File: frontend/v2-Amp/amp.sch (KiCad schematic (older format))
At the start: 69 parts, among them K1 HK4100, P1 Antenna, P2 CONN_02X06, P4 TX-IN, P5 RX IN, P6 12-13.8v, Q1 2N3688A, Q2 RD16HHF1, T1 OUT_TRANSF, T2 OUT_TRANSF, U1 LP2951-50D

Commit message: Completion of Norton addition
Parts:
- removed Q1: 2N3688A, HERMESLITE:TO39EBC, symbol NPN
- removed R13: 51, Resistors_SMD:R_0805_HandSoldering, symbol R
- removed T2: OUT_TRANSF, Pin_Headers:Pin_Header_Straight_2x02, symbol OUT_TRANSF
- added Q1: PZT2222A, TO_SOT_Packages_SMD:SOT-223, symbol PZT2222A-T
- added T2: BN-43-2402, HERMESLITE:TRANSF, symbol TRANSFO2
- R11: value 470 -> 1k
- R18: value 4.7 -> 47
- R9: value 2k -> 1k
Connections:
- wire segments 110 -> 112
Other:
- note added: "1T #30\n"
- note added: "3T #30\n"
- note added: "5T #30\n"
- note added: "Atten R8/12 R10\n dB Ohms Ohms\n 1 910 5.6\n 2 430 12\n 3 270 18\n 4 220 24\n 5 180 30"
- note added: "Attenuator (3db example) needed \nto ensure that input impedance\nof Norton amplifier is 50 ohms."
- note removed: "Attenuator\n(3db example)"
- note removed: "FT37-43\n2x10T #30"
- moved on the sheet: C12, P4, R11, R18, R9
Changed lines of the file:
@@
 	1    0    0    -1
 $EndComp
-Text Notes 4000 3600 0    50   ~ 0
-  Attenuator\n(3db example)
+Text Notes 3450 4650 0    50   ~ 0
+Attenuator (3db example) needed \nto ensure that input impedance\nof Norton amplifier is 50 ohms.
 $Comp
 L INDUCTOR L1
@@
 L CONN_01X02 P4
 U 1 1 55CE52FF
-P 1750 4050
-F 0 "P4" H 1750 4200 50  0000 C CNN
-F 1 "TX-IN" H 1750 3850 50  0000 C CNN
-F 2 "Pin_Headers:Pin_Header_Straight_1x02" H 1750 4050 60  0001 C CNN
-F 3 "" H 1750 4050 60  0000 C CNN
-	1    1750 4050
+P 1250 3950
+F 0 "P4" H 1250 4100 50  0000 C CNN
+F 1 "TX-IN" H 1250 3750 50  0000 C CNN
+F 2 "Pin_Headers:Pin_Header_Straight_1x02" H 1250 3950 60  0001 C CNN
+F 3 "" H 1250 3950 60  0000 C CNN
+	1    1250 3950
 	-1   0    0    1
 $EndComp
@@
 $EndComp
 Wire Wire Line
-	1950 4100 2000 4100
-Wire Wire Line
-	2000 4100 2000 4200
+	1450 4000 1500 4000
+Wire Wire Line
+	1500 4000 1500 4100
 $Comp
 L GND #PWR017
 U 1 1 55D1DC89
-P 2000 4200
-F 0 "#PWR017" H 2000 4200 30  0001 C CNN
-F 1 "GND" H 2000 4130 30  0001 C CNN
-F 2 "" H 2000 4200 60  0000 C CNN
-F 3 "" H 2000 4200 60  0000 C CNN
-	1    2000 4200
+P 1500 4100
+F 0 "#PWR017" H 1500 4100 30  0001 C CNN
+F 1 "GND" H 1500 4030 30  0001 C CNN
+F 2 "" H 1500 4100 60  0000 C CNN
+F 3 "" H 1500 4100 60  0000 C CNN
+	1    1500 4100
 	1    0    0    -1
 $EndComp
@@
 	2150 1250 8800 1250
 $Comp
-L NPN Q1
-U 1 1 55E46016
-P 2550 4000
-F 0 "Q1" H 2550 3850 50  0000 R CNN
-F 1 "2N3688A" H 3050 3850 50  0000 R CNN
-F 2 "HERMESLITE:TO39EBC" H 2550 4000 60  0001 C CNN
-F 3 "" H 2550 4000 60  0000 C CNN
-	1    2550 4000
-	1    0    0    -1
-$EndComp
-$Comp
 L R R9
 U 1 1 55E46597
-P 2350 3750
-F 0 "R9" V 2430 3750 40  0000 C CNN
-F 1 "2k" V 2357 3751 40  0000 C CNN
-F 2 "Resistors_SMD:R_0805_HandSoldering" V 2280 3750 30  0001 C CNN
-F 3 "" H 2350 3750 30  0000 C CNN
-	1    2350 3750
+P 2250 4300
+F 0 "R9" V 2330 4300 40  0000 C CNN
+F 1 "1k" V 2257 4301 40  0000 C CNN
+F 2 "Resistors_SMD:R_0805_HandSoldering" V 2180 4300 30  0001 C CNN
+F 3 "" H 2250 4300 30  0000 C CNN
+	1    2250 4300
 	-1   0    0    1
 $EndComp
@@
 L R R11
 U 1 1 55E46614
-P 2350 4250
-F 0 "R11" V 2430 4250 40  0000 C CNN
-F 1 "470" V 2357 4251 40  0000 C CNN
-F 2 "Resistors_SMD:R_0805_HandSoldering" V 2280 4250 30  0001 C CNN
-F 3 "" H 2350 4250 30  0000 C CNN
-	1    2350 4250
+P 2250 4800
+F 0 "R11" V 2150 4800 40  0000 C CNN
+F 1 "1k" V 2257 4801 40  0000 C CNN
+F 2 "Resistors_SMD:R_0805_HandSoldering" V 2180 4800 30  0001 C CNN
+F 3 "" H 2250 4800 30  0000 C CNN
+	1    2250 4800
 	-1   0    0    1
 $EndComp
@@
 L C C12
 U 1 1 55E46682
-P 2150 4000
-F 0 "C12" V 2200 4050 40  0000 L CNN
-F 1 "0.1uF" H 2150 3900 40  0000 L CNN
-F 2 "HERMESLITE:C_0805" H 2188 3850 30  0001 C CNN
-F 3 "" H 2150 4000 60  0000 C CNN
-	1    2150 4000
+P 1650 3900
+F 0 "C12" V 1700 3950 40  0000 L CNN
+F 1 "0.1uF" V 1750 3650 40  0000 L CNN
+F 2 "HERMESLITE:C_0805" H 1688 3750 30  0001 C CNN
+F 3 "" H 1650 3900 60  0000 C CNN
+	1    1650 3900
 	0    -1   -1   0
 $EndComp
 Connection ~ 3650 1250
-$Comp
-L OUT_TRANSF T2
-U 1 1 55E46E76
-P 3150 3500
-F 0 "T2" H 3150 3750 70  0000 C CNN
-F 1 "OUT_TRANSF" H 3150 3200 70  0000 C CNN
-F 2 "Pin_Headers:Pin_Header_Straight_2x02" H 3150 3500 60  0001 C CNN
-F 3 "" H 3150 3500 60  0000 C CNN
-	1    3150 3500
-	1    0    0    -1
-$EndComp
-Wire Wire Line
-	2650 3500 2650 3800
-Wire Wire Line
-	2650 3700 2750 3700
-Wire Wire Line
-	2650 3500 2350 3500
-Connection ~ 2650 3700
 $Comp
 L C C86
@@
 P 3750 3700
 F 0 "C86" V 3800 3750 40  0000 L CNN
-F 1 "0.1uF" H 3750 3600 40  0000 L CNN
+F 1 "0.1uF" V 3850 3450 40  0000 L CNN
 F 2 "HERMESLITE:C_0805" H 3788 3550 30  0001 C CNN
 F 3 "" H 3750 3700 60  0000 C CNN
@@
 	3800 3300 3550 3300
 Connection ~ 3800 1600
-Wire Wire Line
-	3550 3700 3550 3500
-Wire Wire Line
-	3550 3500 3600 3500
-Wire Wire Line
-	3600 3500 3600 3100
-Wire Wire Line
-	3600 3100 2750 3100
-Wire Wire Line
-	2750 3100 2750 3300
 $Comp
 L C C87
@@
 $EndComp
 Wire Wire Line
-	2650 4200 2650 4250
-Wire Wire Line
-	2550 4250 2750 4250
-Wire Wire Line
-	2550 4250 2550 4350
-Wire Wire Line
-	2750 4250 2750 4350
-Connection ~ 2650 4250
-$Comp
-L R R13
-U 1 1 55E4824A
-P 2550 4600
-F 0 "R13" V 2630 4600 40  0000 C CNN
-F 1 "51" V 2557 4601 40  0000 C CNN
-F 2 "Resistors_SMD:R_0805_HandSoldering" V 2480 4600 30  0001 C CNN
-F 3 "" H 2550 4600 30  0000 C CNN
-	1    2550 4600
-	-1   0    0    1
-$EndComp
+	2550 4750 2550 4800
 $Comp
 L R R18
 U 1 1 55E483BD
-P 2750 4600
-F 0 "R18" V 2830 4600 40  0000 C CNN
-F 1 "4.7" V 2757 4601 40  0000 C CNN
-F 2 "Resistors_SMD:R_0805_HandSoldering" V 2680 4600 30  0001 C CNN
-F 3 "" H 2750 4600 30  0000 C CNN
-	1    2750 4600
-	-1   0    0    1
-$EndComp
-$Comp
-L C C85
-U 1 1 55E484B3
-P 2750 5050
-F 0 "C85" V 2800 5100 40  0000 L CNN
-F 1 "0.1uF" H 2750 4950 40  0000 L CNN
-F 2 "HERMESLITE:C_0805" H 2788 4900 30  0001 C CNN
-F 3 "" H 2750 5050 60  0000 C CNN
-	1    2750 5050
+P 2550 5050
+F 0 "R18" V 2630 5050 40  0000 C CNN
+F 1 "47" V 2557 5051 40  0000 C CNN
+F 2 "Resistors_SMD:R_0805_HandSoldering" V 2480 5050 30  0001 C CNN
+F 3 "" H 2550 5050 30  0000 C CNN
+	1    2550 5050
 	-1   0    0    1
 $EndComp
@@
 L GND #PWR029
 U 1 1 55E488C1
-P 2350 4500
-F 0 "#PWR029" H 2350 4500 30  0001 C CNN
-F 1 "GND" H 2350 4430 30  0001 C CNN
-F 2 "" H 2350 4500 60  0000 C CNN
-F 3 "" H 2350 4500 60  0000 C CNN
-	1    2350 4500
+P 2250 5050
+F 0 "#PWR029" H 2250 5050 30  0001 C CNN
+F 1 "GND" H 2250 4980 30  0001 C CNN
+F 2 "" H 2250 5050 60  0000 C CNN
+F 3 "" H 2250 5050 60  0000 C CNN
+	1    2250 5050
 	1    0    0    -1
 $EndComp
@@
 L GND #PWR030
 U 1 1 55E48911
-P 2750 5250
-F 0 "#PWR030" H 2750 5250 30  0001 C CNN
-F 1 "GND" H 2750 5180 30  0001 C CNN
-F 2 "" H 2750 5250 60  0000 C CNN
-F 3 "" H 2750 5250 60  0000 C CNN
-	1    2750 5250
-	1    0    0    -1
-$EndComp
-$Comp
-L GND #PWR031
-U 1 1 55E48961
-P 2550 4850
-F 0 "#PWR031" H 2550 4850 30  0001 C CNN
-F 1 "GND" H 2550 4780 30  0001 C CNN
-F 2 "" H 2550 4850 60  0000 C CNN
-F 3 "" H 2550 4850 60  0000 C CNN
-	1    2550 4850
-	1    0    0    -1
-$EndComp
-Text Notes 3100 4050 0    50   ~ 0
-FT37-43\n2x10T #30
+P 2550 5300
+F 0 "#PWR030" H 2550 5300 30  0001 C CNN
+F 1 "GND" H 2550 5230 30  0001 C CNN
+F 2 "" H 2550 5300 60  0000 C CNN
+F 3 "" H 2550 5300 60  0000 C CNN
+	1    2550 5300
+	1    0    0    -1
+$EndComp
 Wire Wire Line
 	2400 2500 3250 2500
@@
 Wire Wire Line
 	1700 2000 1900 2000
+$Comp
+L PZT2222A-T Q1
+U 1 1 55E99EC8
+P 2450 4550
+F 0 "Q1" H 2450 4402 40  0000 R CNN
+F 1 "PZT2222A" H 2700 4800 40  0000 R CNN
+F 2 "TO_SOT_Packages_SMD:SOT-223" H 3000 4250 29  0001 C CNN
+F 3 "" H 2450 4550 60  0000 C CNN
+	1    2450 4550
+	1    0    0    -1
+$EndComp
+Wire Wire Line
+	2550 4350 3650 4350
+$Comp
+L C C85
+U 1 1 55EA0F85
+P 2050 4750
+F 0 "C85" V 2100 4800 40  0000 L CNN
+F 1 "0.1uF" H 1850 4650 40  0000 L CNN
+F 2 "HERMESLITE:C_0805" H 2088 4600 30  0001 C CNN
+F 3 "" H 2050 4750 60  0000 C CNN
+	1    2050 4750
+	1    0    0    -1
+$EndComp
+$Comp
+L GND #PWR031
+U 1 1 55EA100D
+P 2050 4950
+F 0 "#PWR031" H 2050 4950 30  0001 C CNN
+F 1 "GND" H 2050 4880 30  0001 C CNN
+F 2 "" H 2050 4950 60  0000 C CNN
+F 3 "" H 2050 4950 60  0000 C CNN
+	1    2050 4950
+	1    0    0    -1
+$EndComp
+Wire Wire Line
+	2050 4550 2250 4550
+$Comp
+L TRANSFO2 T2
+U 1 1 55EA135A
+P 3150 3700
+F 0 "T2" H 3150 4200 70  0000 C CNN
+F 1 "BN-43-2402" H 3200 3150 70  0000 C CNN
+F 2 "HERMESLITE:TRANSF" H 3150 3700 60  0001 C CNN
+F 3 "" H 3150 3700 60  0000 C CNN
+	1    3150 3700
+	1    0    0    -1
+$EndComp
+Wire Wire Line
+	3550 3600 3550 3800
+Connection ~ 3550 3700
+Wire Wire Line
+	3650 4350 3650 4100
+Wire Wire Line
+	3650 4100 3550 4100
+Connection ~ 2650 4350
+Wire Wire Line
+	4850 3100 2250 3100
+Wire Wire Line
+	2250 3100 2250 4050
+Connection ~ 4850 3100
+Wire Wire Line
+	2750 3900 1850 3900
+Wire Wire Line
+	2750 3500 2700 3500
+Wire Wire Line
+	2700 3500 2700 4250
+Wire Wire Line
+	2700 4250 2750 4250
+Wire Wire Line
+	2750 4250 2750 4800
+Wire Wire Line
+	2750 4800 2550 4800
+Connection ~ 2800 3950
+Connection ~ 3500 3550
+Connection ~ 3500 4150
+Text Notes 2750 3750 0    50   ~ 0
+1T #30\n
+Text Notes 3350 3950 0    50   ~ 0
+5T #30\n
+Text Notes 3350 3450 0    50   ~ 0
+3T #30\n
+Text Notes 3600 5250 0    50   ~ 0
+Atten   R8/12     R10\n  dB    Ohms    Ohms\n   1      910      5.6\n   2      430      12\n   3      270      18\n   4      220      24\n   5      180      30
 $EndSCHEMATC

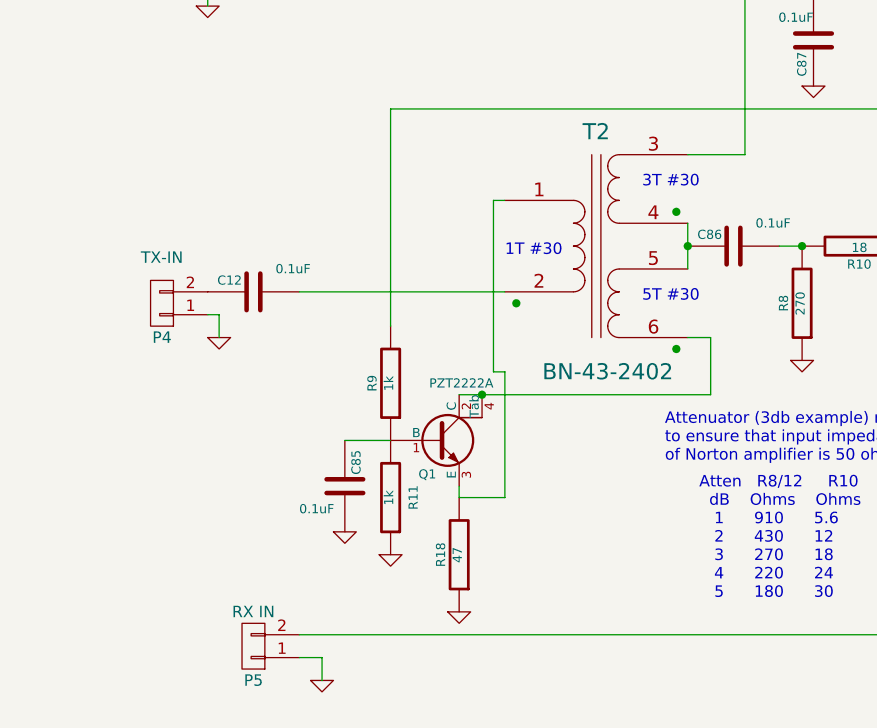
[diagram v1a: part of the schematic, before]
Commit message: additional R added in preamp
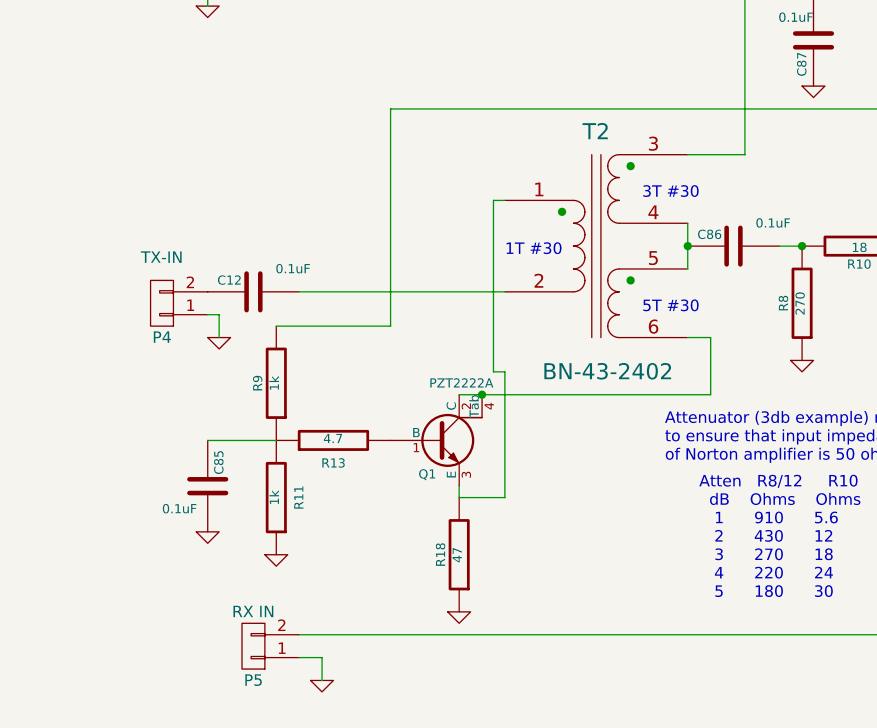
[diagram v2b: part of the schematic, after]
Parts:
- added R13: 4.7, Resistors_SMD:R_0805_HandSoldering, symbol R
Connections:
- net at C85.1, R11.2, R9.1: now also R13.1; no longer Q1.1 (B)
- new net: Q1.1 (B), R13.2
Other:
- moved on the sheet: C85, R11, R9
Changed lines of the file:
@@
 Sheet 1 2
 Title "Hermes-Lite pre-v2 5W Power Amplifier"
-Date "27 August 2015"
+Date "06 September 2015"
 Rev "1.0"
 Comp "SofterHardware"
@@
 L R R9
 U 1 1 55E46597
-P 2250 4300
-F 0 "R9" V 2330 4300 40  0000 C CNN
-F 1 "1k" V 2257 4301 40  0000 C CNN
-F 2 "Resistors_SMD:R_0805_HandSoldering" V 2180 4300 30  0001 C CNN
-F 3 "" H 2250 4300 30  0000 C CNN
-	1    2250 4300
+P 1750 4300
+F 0 "R9" V 1830 4300 40  0000 C CNN
+F 1 "1k" V 1757 4301 40  0000 C CNN
+F 2 "Resistors_SMD:R_0805_HandSoldering" V 1680 4300 30  0001 C CNN
+F 3 "" H 1750 4300 30  0000 C CNN
+	1    1750 4300
 	-1   0    0    1
 $EndComp
@@
 L R R11
 U 1 1 55E46614
-P 2250 4800
-F 0 "R11" V 2150 4800 40  0000 C CNN
-F 1 "1k" V 2257 4801 40  0000 C CNN
-F 2 "Resistors_SMD:R_0805_HandSoldering" V 2180 4800 30  0001 C CNN
-F 3 "" H 2250 4800 30  0000 C CNN
-	1    2250 4800
+P 1750 4800
+F 0 "R11" V 1650 4800 40  0000 C CNN
+F 1 "1k" V 1757 4801 40  0000 C CNN
+F 2 "Resistors_SMD:R_0805_HandSoldering" V 1680 4800 30  0001 C CNN
+F 3 "" H 1750 4800 30  0000 C CNN
+	1    1750 4800
 	-1   0    0    1
 $EndComp
@@
 L GND #PWR029
 U 1 1 55E488C1
-P 2250 5050
-F 0 "#PWR029" H 2250 5050 30  0001 C CNN
-F 1 "GND" H 2250 4980 30  0001 C CNN
-F 2 "" H 2250 5050 60  0000 C CNN
-F 3 "" H 2250 5050 60  0000 C CNN
-	1    2250 5050
+P 1750 5050
+F 0 "#PWR029" H 1750 5050 30  0001 C CNN
+F 1 "GND" H 1750 4980 30  0001 C CNN
+F 2 "" H 1750 5050 60  0000 C CNN
+F 3 "" H 1750 5050 60  0000 C CNN
+	1    1750 5050
 	1    0    0    -1
 $EndComp
@@
 L C C85
 U 1 1 55EA0F85
-P 2050 4750
-F 0 "C85" V 2100 4800 40  0000 L CNN
-F 1 "0.1uF" H 1850 4650 40  0000 L CNN
-F 2 "HERMESLITE:C_0805" H 2088 4600 30  0001 C CNN
-F 3 "" H 2050 4750 60  0000 C CNN
-	1    2050 4750
+P 1450 4750
+F 0 "C85" V 1500 4800 40  0000 L CNN
+F 1 "0.1uF" H 1250 4650 40  0000 L CNN
+F 2 "HERMESLITE:C_0805" H 1488 4600 30  0001 C CNN
+F 3 "" H 1450 4750 60  0000 C CNN
+	1    1450 4750
 	1    0    0    -1
 $EndComp
@@
 L GND #PWR031
 U 1 1 55EA100D
-P 2050 4950
-F 0 "#PWR031" H 2050 4950 30  0001 C CNN
-F 1 "GND" H 2050 4880 30  0001 C CNN
-F 2 "" H 2050 4950 60  0000 C CNN
-F 3 "" H 2050 4950 60  0000 C CNN
-	1    2050 4950
-	1    0    0    -1
-$EndComp
-Wire Wire Line
-	2050 4550 2250 4550
+P 1450 4950
+F 0 "#PWR031" H 1450 4950 30  0001 C CNN
+F 1 "GND" H 1450 4880 30  0001 C CNN
+F 2 "" H 1450 4950 60  0000 C CNN
+F 3 "" H 1450 4950 60  0000 C CNN
+	1    1450 4950
+	1    0    0    -1
+$EndComp
 $Comp
 L TRANSFO2 T2
@@
 Wire Wire Line
 	2750 4800 2550 4800
-Connection ~ 2800 3950
-Connection ~ 3500 3550
-Connection ~ 3500 4150
+Connection ~ 3000 3550
+Connection ~ 3300 3350
+Connection ~ 3300 3850
 Text Notes 2750 3750 0    50   ~ 0
 1T #30\n
-Text Notes 3350 3950 0    50   ~ 0
+Text Notes 3350 4000 0    50   ~ 0
 5T #30\n
-Text Notes 3350 3450 0    50   ~ 0
+Text Notes 3350 3500 0    50   ~ 0
 3T #30\n
 Text Notes 3600 5250 0    50   ~ 0
 Atten   R8/12     R10\n  dB    Ohms    Ohms\n   1      910      5.6\n   2      430      12\n   3      270      18\n   4      220      24\n   5      180      30
+$Comp
+L R R13
+U 1 1 55EC27CC
+P 2000 4550
+F 0 "R13" V 1900 4550 40  0000 C CNN
+F 1 "4.7" V 2007 4551 40  0000 C CNN
+F 2 "Resistors_SMD:R_0805_HandSoldering" V 1930 4550 30  0001 C CNN
+F 3 "" H 2000 4550 30  0000 C CNN
+	1    2000 4550
+	0    -1   -1   0
+$EndComp
+Wire Wire Line
+	2250 4050 1750 4050
+Wire Wire Line
+	1450 4550 1750 4550
 $EndSCHEMATC
